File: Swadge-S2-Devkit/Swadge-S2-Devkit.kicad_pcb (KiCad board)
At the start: 2 copper layers, 99.9 x 99.9 mm, 83 parts, among them J1 USB_B_Micro, J2 DEBUG_BANK_C, J3 DEBUG_BANK_B, J4 DEBUG_BANK_A, J5 MICSEL, J6 TRYMIC, M1 Motor_DC, Q1 Q_N_FET, Q2 AP2003_PN_FET, Q3 AP2003_PN_FET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

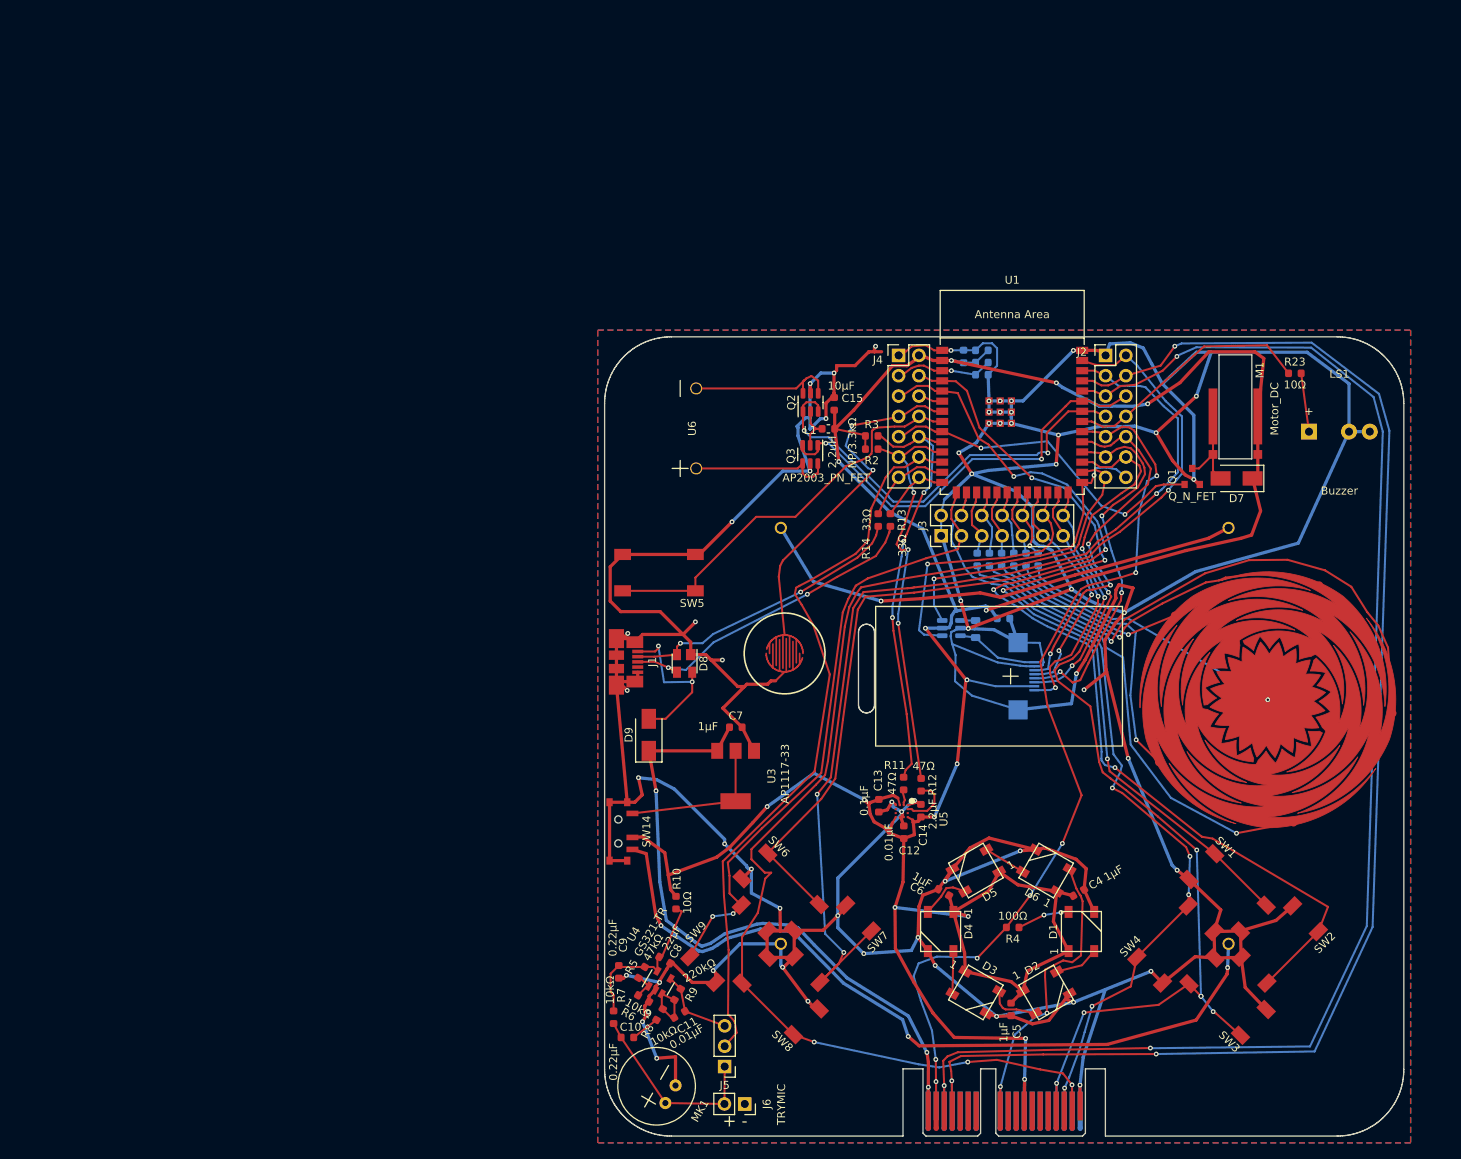
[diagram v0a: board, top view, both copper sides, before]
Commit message: Switched to controller PCB
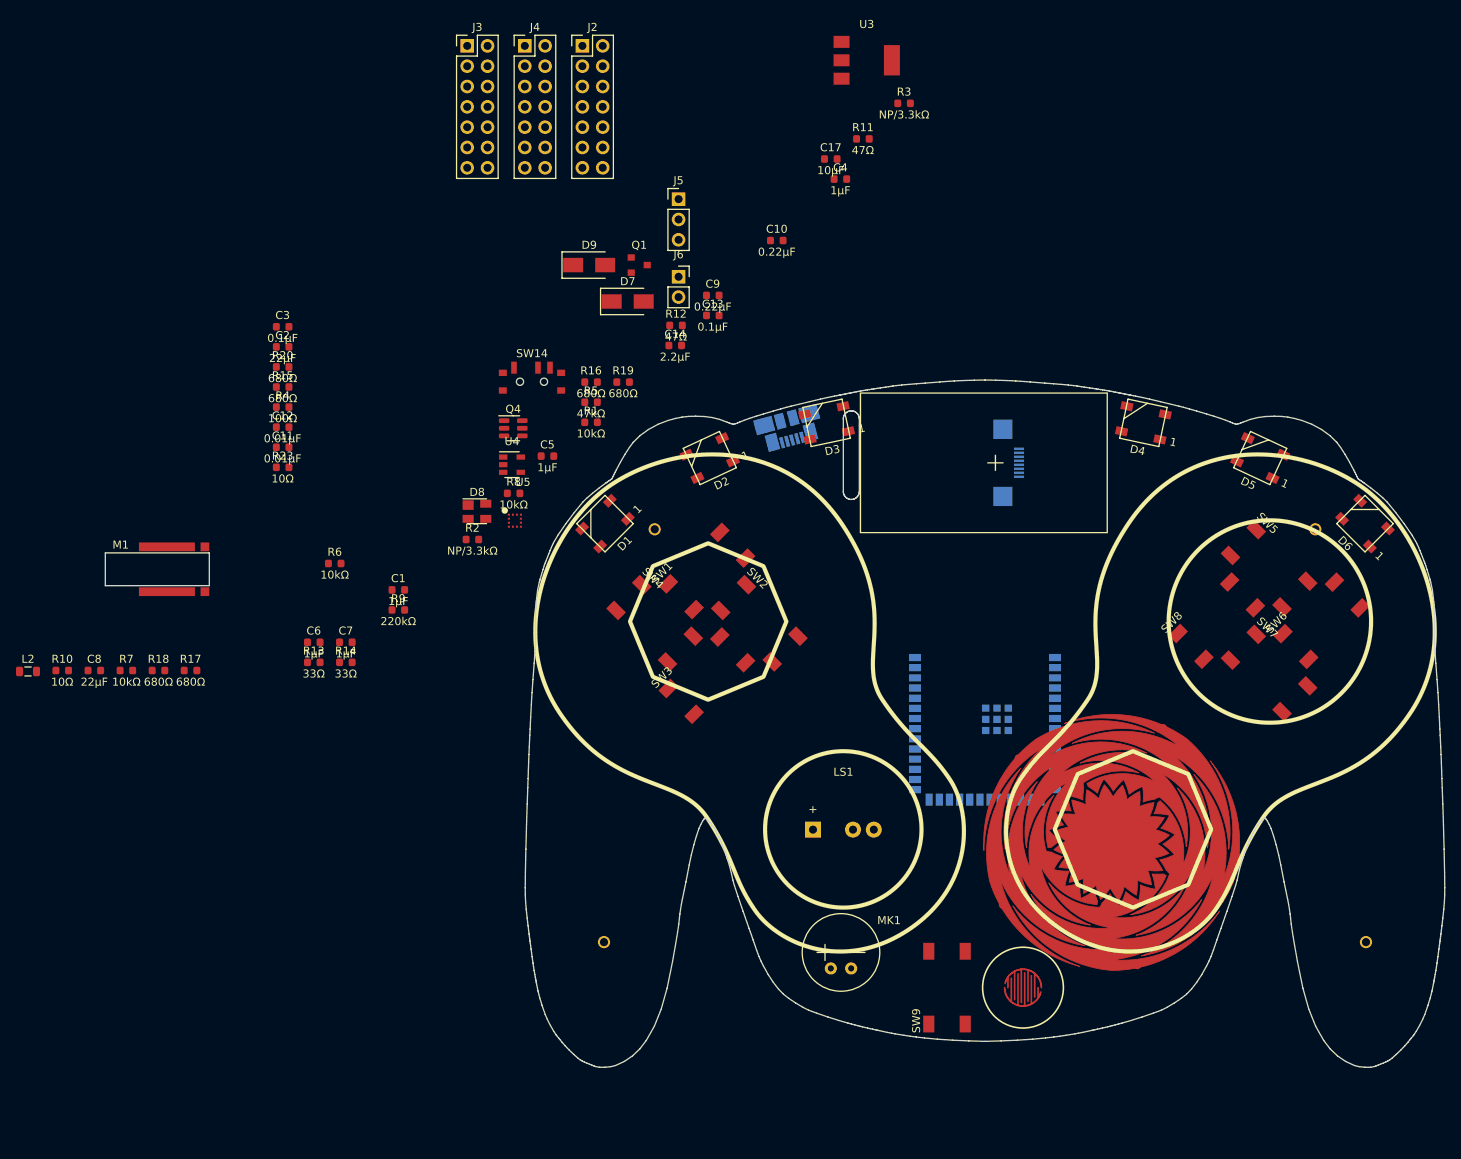
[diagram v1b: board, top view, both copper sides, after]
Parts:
- removed C15: 10μF, Swadge_Parts:C_0603_1608Metric
- removed L1: 2.2uH, Swadge_Parts:L_0603_1608Metric
- removed Q2, Q3: AP2003_PN_FET, Swadge_Parts:SOT-23-6
- removed U2: BUS_PCIexpress, Swadge_Parts:BUS_PCIexpress
- removed U6: INGHAi_GSPK2308P-8R0.5W, Swadge_Parts:INGHAi GSPK2308P-8R0.5W
- added G*** (x6): LOGO, LOGO, F.Cu at (150.0, 100.0)
- C1, C17, C2, C3, L2, Q4, R1, R15, R16, R17, R18, R19, R20: moved to F.Cu
- J1, U1: moved to B.Cu
- moved M1 138.9 mm to (44.2, 80.7), turned to 0 degrees
- moved R23 127.1 mm to (62.2, 68.0)
- moved L2 118.6 mm to (30.4, 93.5), turned to 0 degrees
- moved R4 112.1 mm to (62.2, 60.4), turned to 0 degrees
- moved J5 108.6 mm to (111.7, 34.4), turned to 0 degrees
- moved R18 107.8 mm to (46.7, 93.4), turned to 0 degrees
- moved J6 103.7 mm to (111.7, 44.1), turned to 0 degrees
- moved R17 102.3 mm to (50.7, 93.4), turned to 0 degrees
- moved C10 101.4 mm to (124.0, 39.6), turned to 0 degrees
- moved R20 97.5 mm to (62.2, 55.4), turned to 0 degrees
- moved C4 94.0 mm to (131.9, 31.9), turned to 0 degrees
- moved C12 92.7 mm to (62.2, 62.9), turned to 0 degrees
- moved U3 91.0 mm to (135.2, 17.1), turned to 0 degrees
- moved C5 90.2 mm to (95.3, 66.6), turned to 0 degrees
- moved R15 89.5 mm to (62.2, 57.9), turned to 0 degrees
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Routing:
- net GND: track 861.3 -> 0.00 mm, vias 61 -> 0
- net +3V3: track 382.9 -> 0.00 mm, vias 15 -> 0
- net TX: track 180.7 -> 0.00 mm, vias 3 -> 0
- net RX: track 178.9 -> 0.00 mm, vias 3 -> 0
- net BTN_8: track 155.1 -> 0.00 mm, vias 4 -> 0
- net BTN_2: track 127.0 -> 0.00 mm, vias 4 -> 0
- net BTN_7: track 125.7 -> 0.00 mm, vias 3 -> 0
- net BTN_3: track 118.6 -> 0.00 mm, vias 7 -> 0
- net LED: track 115.4 -> 0.00 mm, vias 7 -> 0
- net BTN_6: track 112.6 -> 0.00 mm, vias 1 -> 0
- net BTN_4: track 109.6 -> 0.00 mm, vias 5 -> 0
- net BTN_1: track 103.5 -> 0.00 mm, vias 4 -> 0
- net BATTPLUS: track 96.6 -> 0.00 mm, vias 3 -> 0
- net MIC: track 91.5 -> 0.00 mm
- net +5V: track 84.4 -> 0.00 mm, vias 3 -> 0
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- removed copper zone on B.Cu, net GND
- removed copper zone on F.Cu, net GND
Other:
- board size 99.9 x 99.9 mm -> 114.9 x 85.9 mm
- rule pad_to_mask_clearance: 0 -> 0.2
- board text removed: "+ -"
